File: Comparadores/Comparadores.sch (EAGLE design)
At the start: 6 parts, among them IC1 LM324D

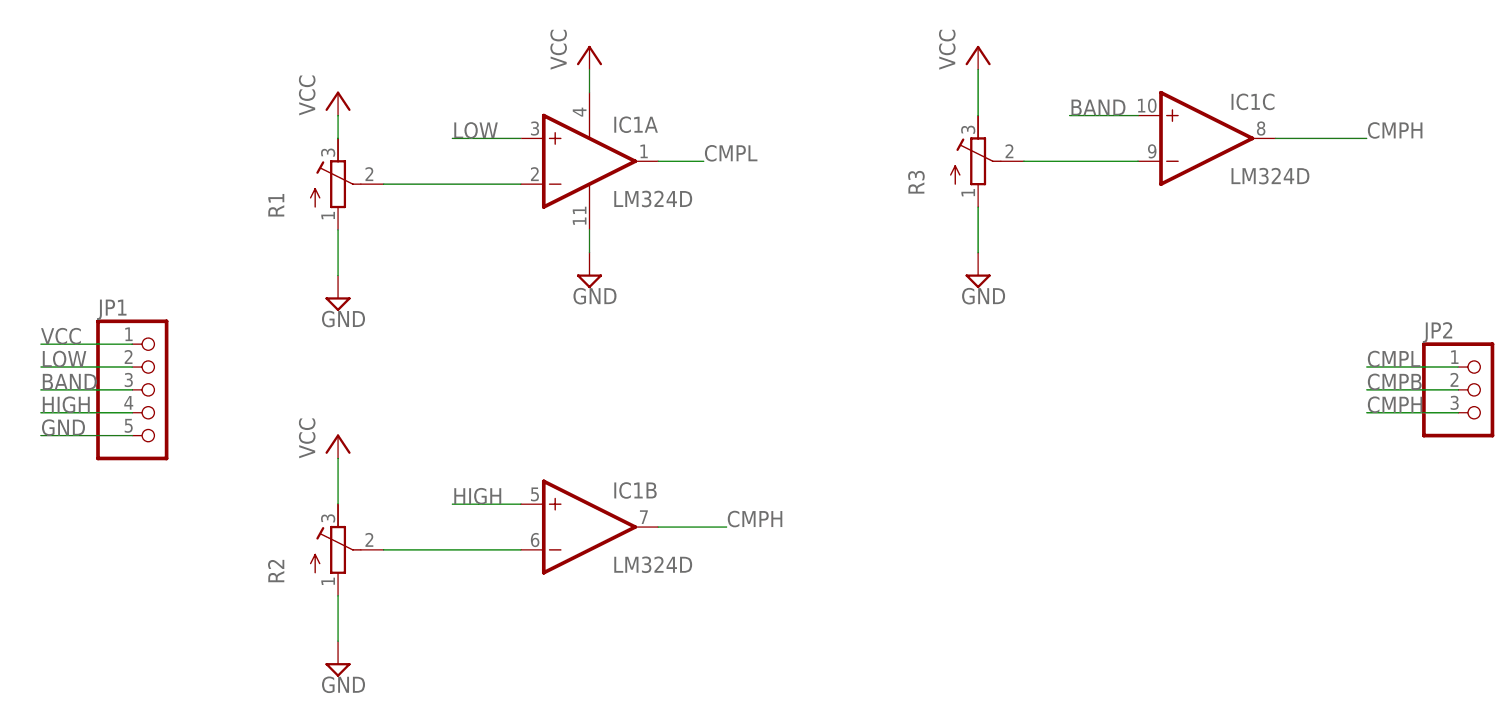
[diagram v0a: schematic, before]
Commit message: Se agregan conexiones y archivos de configuración CNC
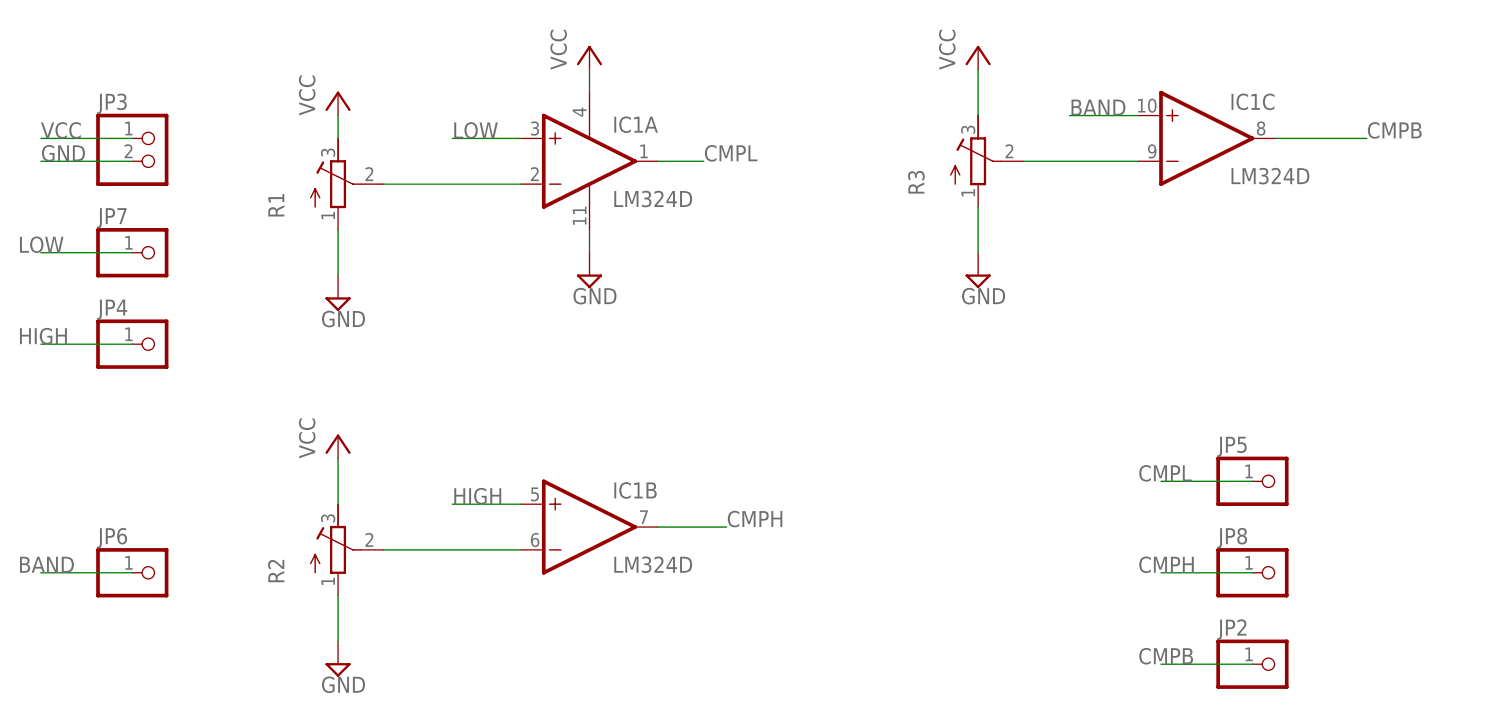
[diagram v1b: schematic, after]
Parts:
- removed JP1: (no value), pinhead:PINHD-1X5
- added JP3: (no value), pinhead:PINHD-1X2
- added JP4, JP5, JP6, JP7, JP8: (no value), pinhead:PINHD-1X1
- JP2: device pinhead:PINHD-1X3 -> pinhead:PINHD-1X1
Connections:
- net BAND: now also JP6.1; no longer JP1.3
- net CMPB: now also IC1C.OUT, JP2.1; no longer JP2.2
- net CMPH: now also JP8.1; no longer IC1C.OUT, JP2.3
- net CMPL: now also JP5.1; no longer JP2.1
- net GND: now also JP3.2; no longer JP1.5
- net HIGH: now also JP4.1; no longer JP1.4
- net LOW: now also JP7.1; no longer JP1.2
- net VCC: now also JP3.1; no longer JP1.1
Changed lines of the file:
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@@
 <part name="SUPPLY4" library="supply2" library_urn="urn:adsk.eagle:library:372" deviceset="GND" device=""/>
 <part name="P+1" library="supply1" library_urn="urn:adsk.eagle:library:371" deviceset="VCC" device=""/>
-<part name="JP1" library="pinhead" library_urn="urn:adsk.eagle:library:325" deviceset="PINHD-1X5" device="" package3d_urn="urn:adsk.eagle:package:22469/2"/>
 <part name="P+2" library="supply1" library_urn="urn:adsk.eagle:library:371" deviceset="VCC" device=""/>
 <part name="P+3" library="supply1" library_urn="urn:adsk.eagle:library:371" deviceset="VCC" device=""/>
 <part name="P+4" library="supply1" library_urn="urn:adsk.eagle:library:371" deviceset="VCC" device=""/>
-<part name="JP2" library="pinhead" library_urn="urn:adsk.eagle:library:325" deviceset="PINHD-1X3" device="" package3d_urn="urn:adsk.eagle:package:22458/2"/>
+<part name="JP3" library="pinhead" library_urn="urn:adsk.eagle:library:325" deviceset="PINHD-1X2" device="" package3d_urn="urn:adsk.eagle:package:22435/2"/>
+<part name="JP5" library="pinhead" library_urn="urn:adsk.eagle:library:325" deviceset="PINHD-1X1" device="" package3d_urn="urn:adsk.eagle:package:22485/2"/>
+<part name="JP6" library="pinhead" library_urn="urn:adsk.eagle:library:325" deviceset="PINHD-1X1" device="" package3d_urn="urn:adsk.eagle:package:22485/2"/>
+<part name="JP4" library="pinhead" library_urn="urn:adsk.eagle:library:325" deviceset="PINHD-1X1" device="" package3d_urn="urn:adsk.eagle:package:22485/2"/>
+<part name="JP7" library="pinhead" library_urn="urn:adsk.eagle:library:325" deviceset="PINHD-1X1" device="" package3d_urn="urn:adsk.eagle:package:22485/2"/>
+<part name="JP2" library="pinhead" library_urn="urn:adsk.eagle:library:325" deviceset="PINHD-1X1" device="" package3d_urn="urn:adsk.eagle:package:22485/2"/>
+<part name="JP8" library="pinhead" library_urn="urn:adsk.eagle:library:325" deviceset="PINHD-1X1" device="" package3d_urn="urn:adsk.eagle:package:22485/2"/>
 </parts>
 <sheets>
@@
 <attribute name="VALUE" x="45.72" y="63.5" size="1.778" layer="96" rot="R90"/>
 </instance>
-<instance part="JP1" gate="A" x="0" y="27.94" smashed="yes">
-<attribute name="NAME" x="-6.35" y="36.195" size="1.778" layer="95"/>
-<attribute name="VALUE" x="-6.35" y="17.78" size="1.778" layer="96"/>
-</instance>
 <instance part="P+2" gate="VCC" x="20.32" y="60.96" smashed="yes">
 <attribute name="VALUE" x="17.78" y="58.42" size="1.778" layer="96" rot="R90"/>
@@
 <attribute name="VALUE" x="88.9" y="63.5" size="1.778" layer="96" rot="R90"/>
 </instance>
-<instance part="JP2" gate="A" x="147.32" y="27.94" smashed="yes">
-<attribute name="NAME" x="140.97" y="33.655" size="1.778" layer="95"/>
-<attribute name="VALUE" x="140.97" y="20.32" size="1.778" layer="96"/>
+<instance part="JP3" gate="G$1" x="0" y="53.34" smashed="yes">
+<attribute name="NAME" x="-6.35" y="59.055" size="1.778" layer="95"/>
+<attribute name="VALUE" x="-6.35" y="48.26" size="1.778" layer="96"/>
+</instance>
+<instance part="JP5" gate="G$1" x="124.46" y="17.78" smashed="yes">
+<attribute name="NAME" x="118.11" y="20.955" size="1.778" layer="95"/>
+<attribute name="VALUE" x="118.11" y="12.7" size="1.778" layer="96"/>
+</instance>
+<instance part="JP6" gate="G$1" x="0" y="7.62" smashed="yes">
+<attribute name="NAME" x="-6.35" y="10.795" size="1.778" layer="95"/>
+<attribute name="VALUE" x="-6.35" y="2.54" size="1.778" layer="96"/>
+</instance>
+<instance part="JP4" gate="G$1" x="0" y="33.02" smashed="yes">
+<attribute name="NAME" x="-6.35" y="36.195" size="1.778" layer="95"/>
+<attribute name="VALUE" x="-6.35" y="27.94" size="1.778" layer="96"/>
+</instance>
+<instance part="JP7" gate="G$1" x="0" y="43.18" smashed="yes">
+<attribute name="NAME" x="-6.35" y="46.355" size="1.778" layer="95"/>
+<attribute name="VALUE" x="-6.35" y="38.1" size="1.778" layer="96"/>
+</instance>
+<instance part="JP2" gate="G$1" x="124.46" y="-2.54" smashed="yes">
+<attribute name="NAME" x="118.11" y="0.635" size="1.778" layer="95"/>
+<attribute name="VALUE" x="118.11" y="-7.62" size="1.778" layer="96"/>
+</instance>
+<instance part="JP8" gate="G$1" x="124.46" y="7.62" smashed="yes">
+<attribute name="NAME" x="118.11" y="10.795" size="1.778" layer="95"/>
+<attribute name="VALUE" x="118.11" y="2.54" size="1.778" layer="96"/>
 </instance>
 </instances>
@@
 </segment>
 <segment>
-<pinref part="JP1" gate="A" pin="1"/>
-<wire x1="-2.54" y1="33.02" x2="-12.7" y2="33.02" width="0.1524" layer="91"/>
-<label x="-12.7" y="33.02" size="1.778" layer="95"/>
+<pinref part="JP3" gate="G$1" pin="1"/>
+<wire x1="-2.54" y1="55.88" x2="-12.7" y2="55.88" width="0.1524" layer="91"/>
+<label x="-12.7" y="55.88" size="1.778" layer="95"/>
 </segment>
 </net>
@@
 </segment>
 <segment>
-<pinref part="JP1" gate="A" pin="5"/>
-<wire x1="-2.54" y1="22.86" x2="-12.7" y2="22.86" width="0.1524" layer="91"/>
-<label x="-12.7" y="22.86" size="1.778" layer="95"/>
+<pinref part="JP3" gate="G$1" pin="2"/>
+<wire x1="-2.54" y1="53.34" x2="-12.7" y2="53.34" width="0.1524" layer="91"/>
+<label x="-12.7" y="53.34" size="1.778" layer="95"/>
 </segment>
 </net>
@@
 <net name="LOW" class="0">
 <segment>
-<pinref part="JP1" gate="A" pin="2"/>
-<wire x1="-2.54" y1="30.48" x2="-12.7" y2="30.48" width="0.1524" layer="91"/>
-<label x="-12.7" y="30.48" size="1.778" layer="95"/>
-</segment>
-<segment>
 <pinref part="IC1" gate="A" pin="+IN"/>
 <wire x1="40.64" y1="55.88" x2="33.02" y2="55.88" width="0.1524" layer="91"/>
 <label x="33.02" y="55.88" size="1.778" layer="95"/>
 </segment>
+<segment>
+<pinref part="JP7" gate="G$1" pin="1"/>
+<wire x1="-2.54" y1="43.18" x2="-12.7" y2="43.18" width="0.1524" layer="91"/>
+<label x="-15.24" y="43.18" size="1.778" layer="95"/>
+</segment>
 </net>
 <net name="BAND" class="0">
-<segment>
-<pinref part="JP1" gate="A" pin="3"/>
-<wire x1="-2.54" y1="27.94" x2="-12.7" y2="27.94" width="0.1524" layer="91"/>
-<label x="-12.7" y="27.94" size="1.778" layer="95"/>
-</segment>
 <segment>
 <pinref part="IC1" gate="C" pin="+IN"/>
@@
 <label x="101.6" y="58.42" size="1.778" layer="95"/>
 </segment>
+<segment>
+<pinref part="JP6" gate="G$1" pin="1"/>
+<wire x1="-2.54" y1="7.62" x2="-12.7" y2="7.62" width="0.1524" layer="91"/>
+<label x="-15.24" y="7.62" size="1.778" layer="95"/>
+</segment>
 </net>
 <net name="HIGH" class="0">
-<segment>
-<pinref part="JP1" gate="A" pin="4"/>
-<wire x1="-2.54" y1="25.4" x2="-12.7" y2="25.4" width="0.1524" layer="91"/>
-<label x="-12.7" y="25.4" size="1.778" layer="95"/>
-</segment>
 <segment>
 <pinref part="IC1" gate="B" pin="+IN"/>
@@
 <label x="33.02" y="15.24" size="1.778" layer="95"/>
 </segment>
+<segment>
+<pinref part="JP4" gate="G$1" pin="1"/>
+<wire x1="-2.54" y1="33.02" x2="-12.7" y2="33.02" width="0.1524" layer="91"/>
+<label x="-15.24" y="33.02" size="1.778" layer="95"/>
+</segment>
 </net>
 <net name="N$16" class="0">
@@
 <net name="CMPL" class="0">
 <segment>
-<pinref part="JP2" gate="A" pin="1"/>
-<wire x1="144.78" y1="30.48" x2="134.62" y2="30.48" width="0.1524" layer="91"/>
-<label x="134.62" y="30.48" size="1.778" layer="95"/>
-</segment>
-<segment>
 <pinref part="IC1" gate="A" pin="OUT"/>
 <wire x1="55.88" y1="53.34" x2="60.96" y2="53.34" width="0.1524" layer="91"/>
 <label x="60.96" y="53.34" size="1.778" layer="95"/>
 </segment>
+<segment>
+<pinref part="JP5" gate="G$1" pin="1"/>
+<wire x1="121.92" y1="17.78" x2="111.76" y2="17.78" width="0.1524" layer="91"/>
+<label x="109.22" y="17.78" size="1.778" layer="95"/>
+</segment>
 </net>
 <net name="CMPB" class="0">
 <segment>
-<pinref part="JP2" gate="A" pin="2"/>
-<wire x1="144.78" y1="27.94" x2="134.62" y2="27.94" width="0.1524" layer="91"/>
-<label x="134.62" y="27.94" size="1.778" layer="95"/>
+<pinref part="IC1" gate="C" pin="OUT"/>
+<wire x1="124.46" y1="55.88" x2="134.62" y2="55.88" width="0.1524" layer="91"/>
+<label x="134.62" y="55.88" size="1.778" layer="95"/>
+</segment>
+<segment>
+<pinref part="JP2" gate="G$1" pin="1"/>
+<wire x1="121.92" y1="-2.54" x2="111.76" y2="-2.54" width="0.1524" layer="91"/>
+<label x="109.22" y="-2.54" size="1.778" layer="95"/>
 </segment>
 </net>
 <net name="CMPH" class="0">
-<segment>
-<pinref part="JP2" gate="A" pin="3"/>
-<wire x1="144.78" y1="25.4" x2="134.62" y2="25.4" width="0.1524" layer="91"/>
-<label x="134.62" y="25.4" size="1.778" layer="95"/>
-</segment>
 <segment>
 <pinref part="IC1" gate="B" pin="OUT"/>
@@
 </segment>
 <segment>
-<pinref part="IC1" gate="C" pin="OUT"/>
-<wire x1="124.46" y1="55.88" x2="134.62" y2="55.88" width="0.1524" layer="91"/>
-<label x="134.62" y="55.88" size="1.778" layer="95"/>
-</segment>
+<pinref part="JP8" gate="G$1" pin="1"/>
+<wire x1="121.92" y1="7.62" x2="111.76" y2="7.62" width="0.1524" layer="91"/>
+<label x="109.22" y="7.62" size="1.778" layer="95"/>
+</segment>
+</net>
+<net name="CMPH1" class="0">
 </net>
 </nets>
